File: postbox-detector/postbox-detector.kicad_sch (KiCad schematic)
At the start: 5 parts

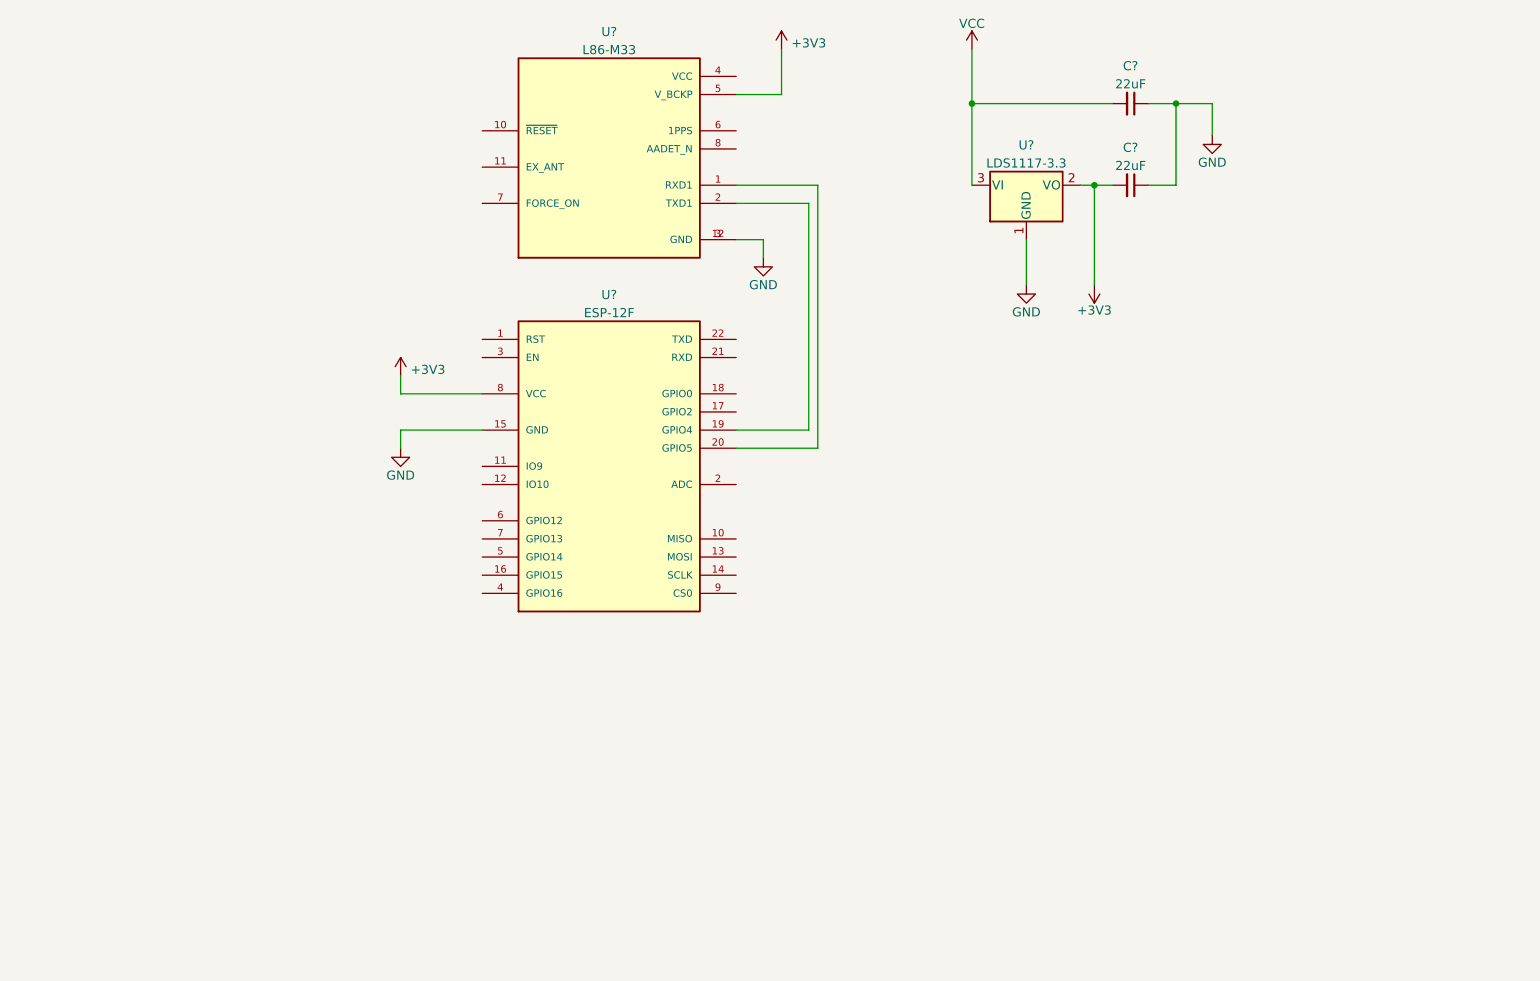
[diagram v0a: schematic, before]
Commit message: crude test implementation and pcb layout
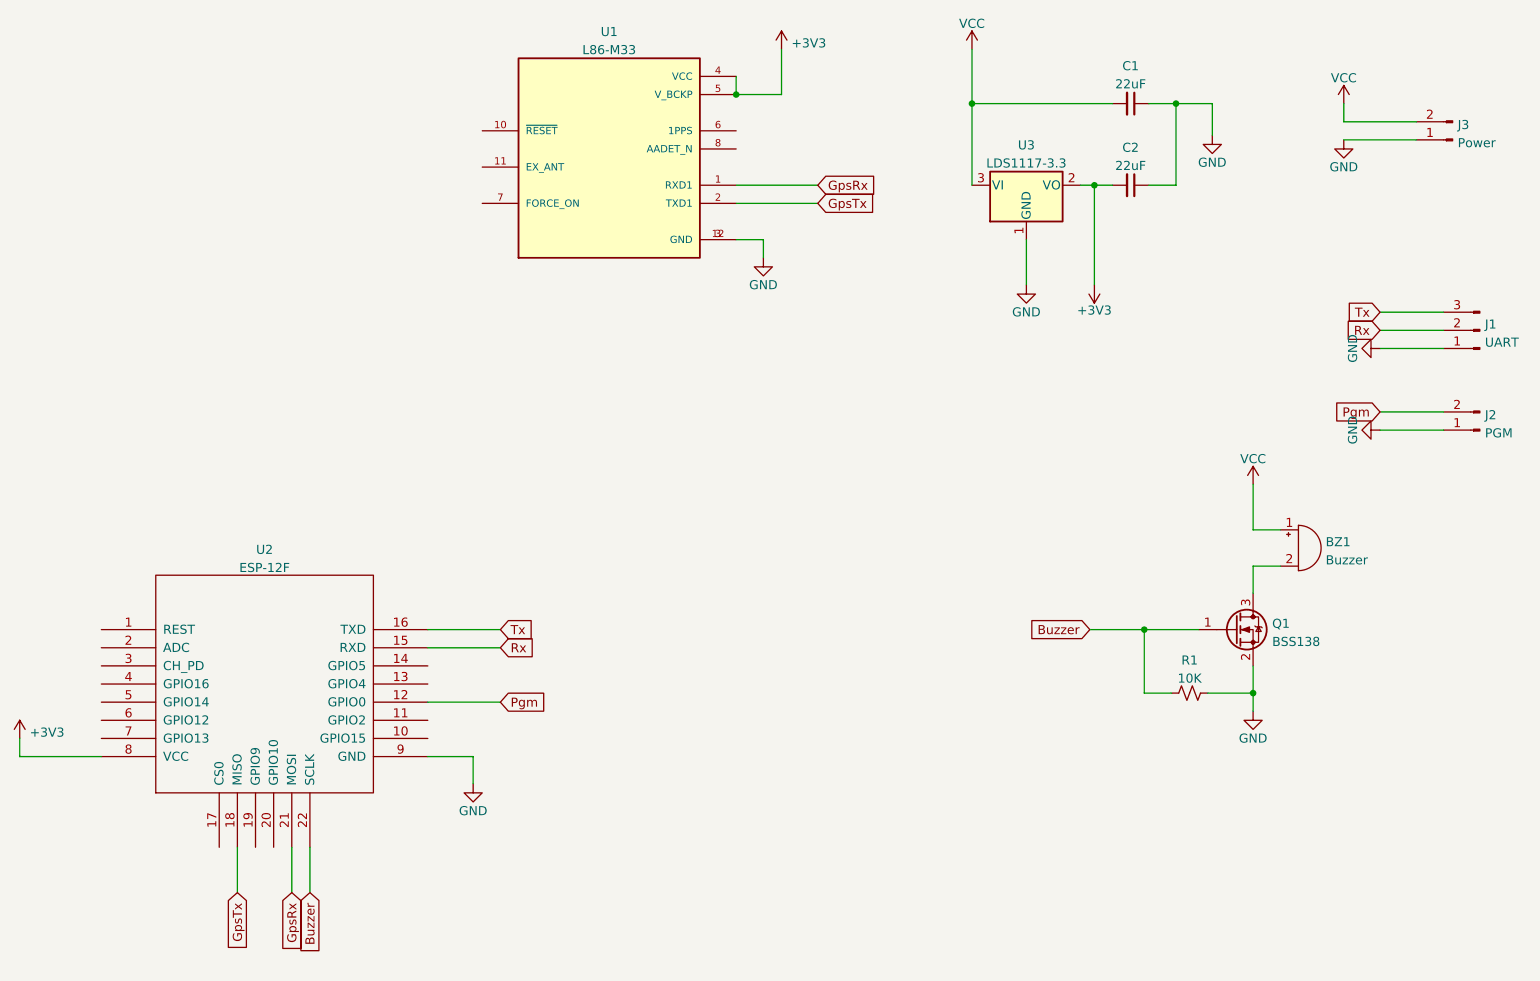
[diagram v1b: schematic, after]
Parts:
- added BZ1: Buzzer, Custom:Buzzer_9.2x4.2_WST-0904T, symbol Device:Buzzer
- added J1: UART, Connector_PinHeader_2.54mm:PinHeader_1x03_P2.54mm_Vertical, symbol Connector:Conn_01x03_Male
- added J2: PGM, Connector_PinHeader_2.54mm:PinHeader_1x02_P2.54mm_Vertical, symbol Connector:Conn_01x02_Male
- added J3: Power, Connector_PinHeader_2.54mm:PinHeader_1x02_P2.54mm_Vertical, symbol Connector:Conn_01x02_Male
- added Q1: BSS138, Package_TO_SOT_SMD:SOT-23, symbol Transistor_FET:BSS138
- added R1: 10K, Resistor_SMD:R_1206_3216Metric, symbol Device:R_Small_US
- U2: renamed from U?; footprint ESP-12F -> ESP8266:ESP-12E; symbol ESP-12F:ESP-12F -> ESP8266:ESP-12F
- gave numbers to parts that had none: 4
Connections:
- net +3V3: now also U1.4 (VCC)
- net GND: now also U2.9 (GND), J1.1 (Pin_1), J2.1 (Pin_1), J3.1 (Pin_1), Q1.2 (S), R1.1; no longer U2.15 (GND)
- net VCC: now also BZ1.1 (-), J3.2 (Pin_2)
- net at U2.20 (GPIO10): no longer U1.1 (RXD1)
- net at U2.19 (GPIO9): no longer U1.2 (TXD1)
- net Pgm: now reaches U2.12 (GPIO0)
- net Pgm: now also J2.2 (Pin_2)
- net Tx: now reaches U2.16 (TXD)
- net Tx: now also J1.3 (Pin_3)
- net GpsTx: now reaches U2.18 (MISO)
- net GpsTx: now also U1.2 (TXD1)
- net GpsRx: now reaches U2.21 (MOSI)
- net GpsRx: now also U1.1 (RXD1)
- net Buzzer: now reaches U2.22 (SCLK)
- net Buzzer: now also Q1.1 (G), R1.2
- new net: BZ1.2 (+), Q1.3 (D)
- new net Rx: J1.2 (Pin_2), U2.15 (RXD)
